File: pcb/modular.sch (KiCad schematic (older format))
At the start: 40 parts

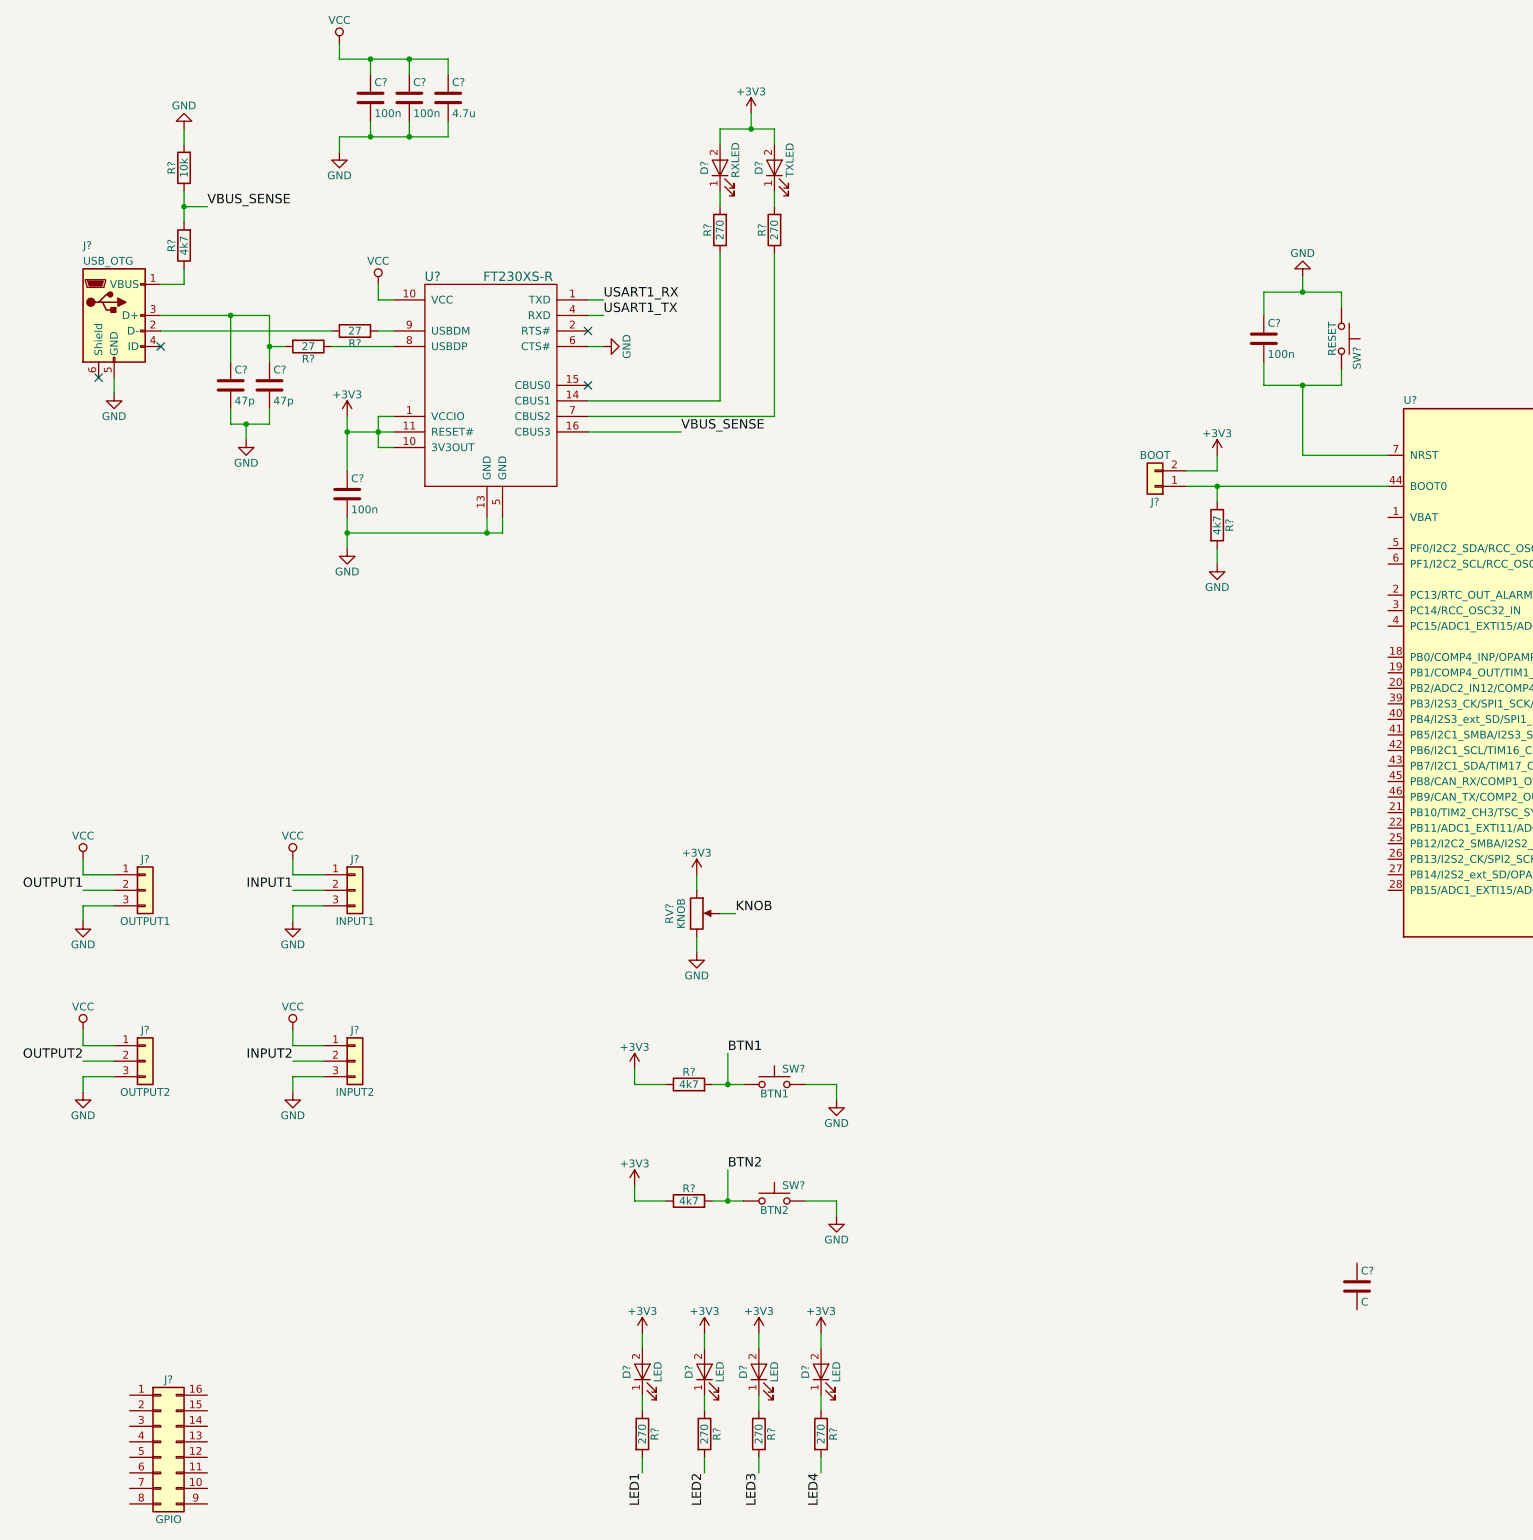
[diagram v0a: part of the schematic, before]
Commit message: Added pcb layout
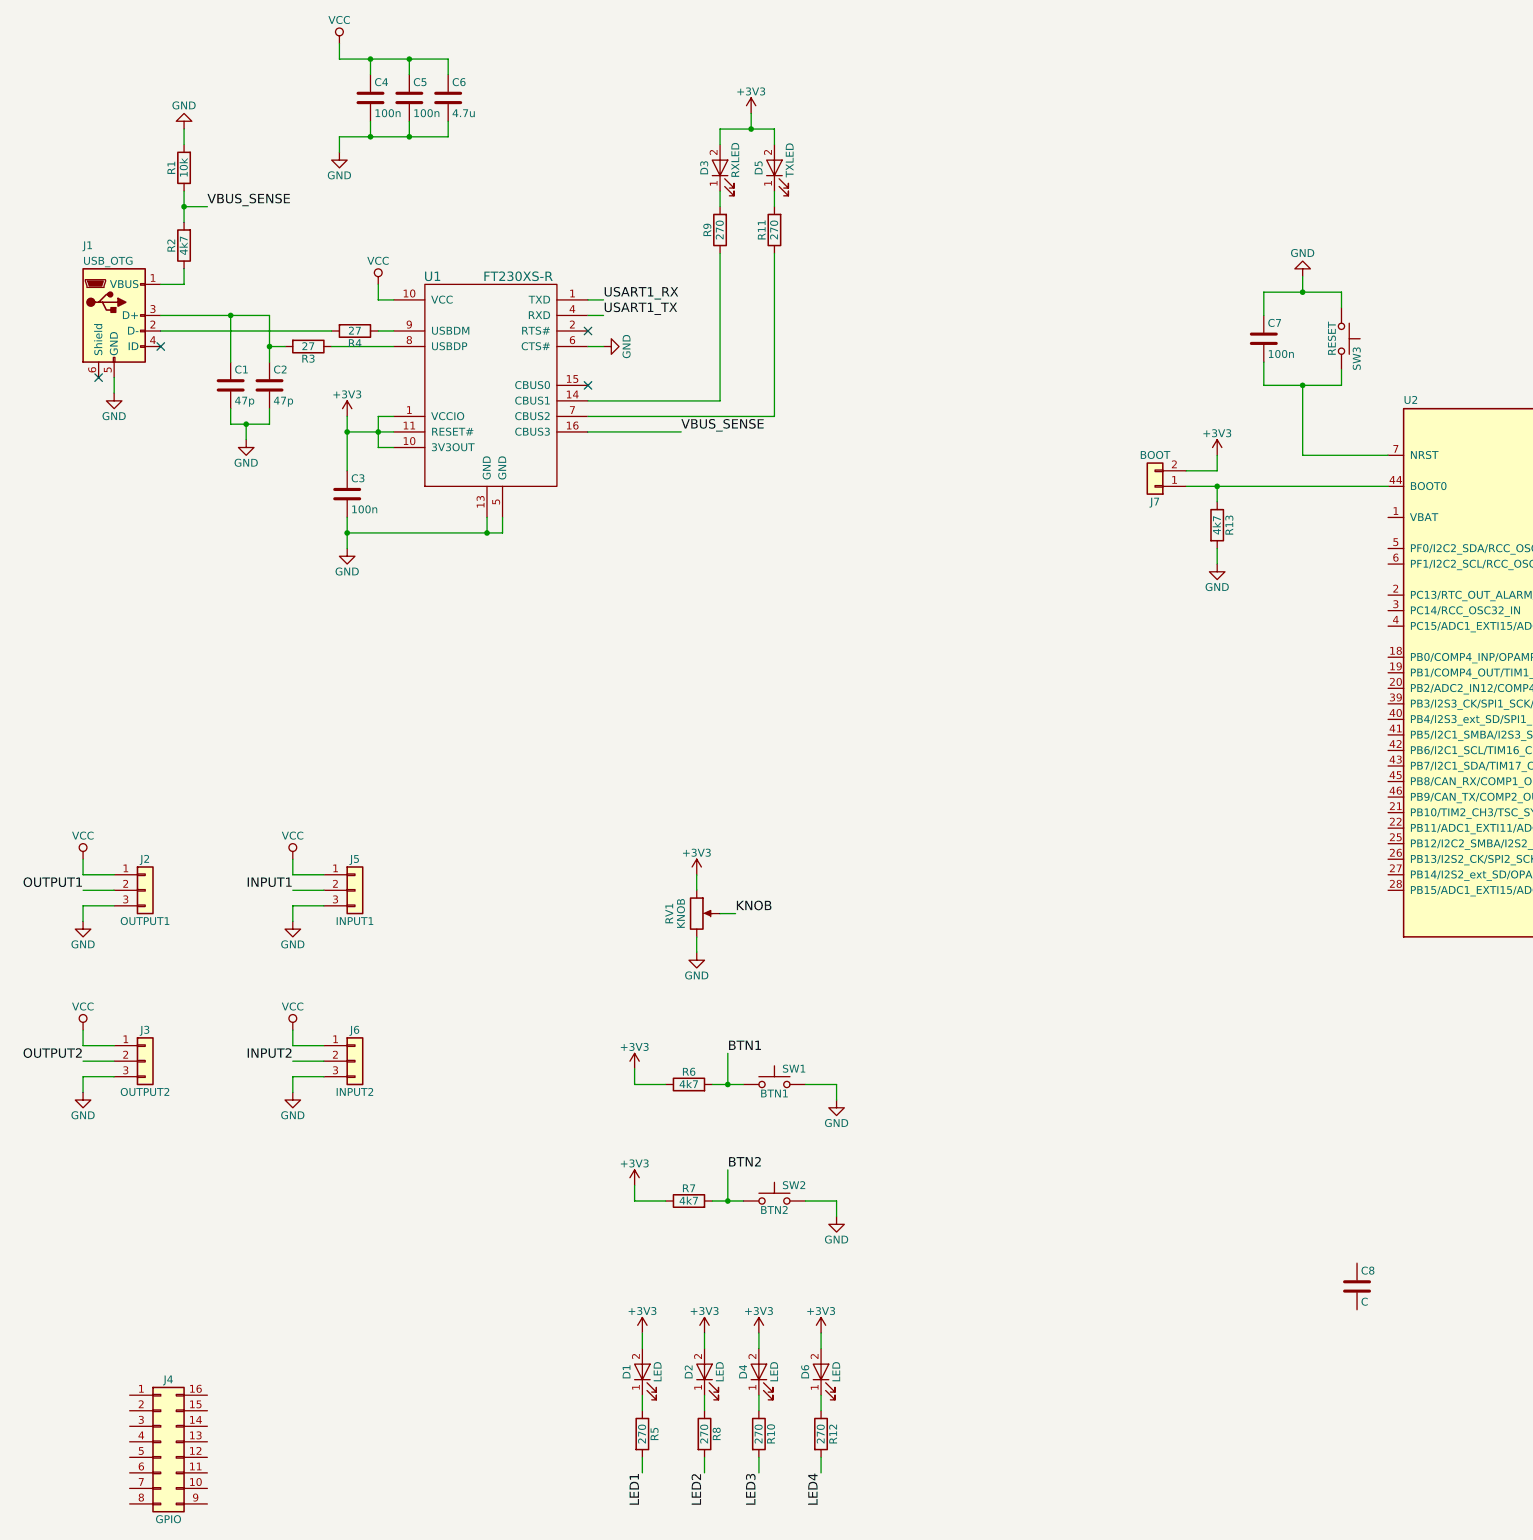
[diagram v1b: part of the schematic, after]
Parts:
- C1, C2, C3, C4, C5, C6, C7, C8: renamed from C?; footprint (none) -> Capacitors_SMD:C_1210_HandSoldering
- D1, D2, D3, D4, D5, D6: renamed from D?; footprint (none) -> LEDs:LED_1206_HandSoldering
- J1: renamed from J?; footprint (none) -> Connectors_USB:USB_Micro-B_Molex-105017-0001
- J2, J3, J5, J6: renamed from J?; footprint (none) -> Pin_Headers:Pin_Header_Straight_1x03_Pitch2.54mm
- J4: renamed from J?; footprint (none) -> Pin_Headers:Pin_Header_Straight_2x08_Pitch2.54mm
- J7: renamed from J?; footprint (none) -> Pin_Headers:Pin_Header_Straight_1x02_Pitch2.54mm
- R1, R10, R11, R12, R13, R2, R3, R4, R5, R6, R7, R8, R9: renamed from R?; footprint (none) -> Resistors_SMD:R_1210_HandSoldering
- RV1: renamed from RV?; footprint (none) -> Potentiometers:Potentiometer_Alps_RK09K_Vertical
- SW1, SW2, SW3: renamed from SW?; footprint (none) -> Buttons_Switches_THT:SW_PUSH_6mm
- U1: renamed from U?; footprint (none) -> Housings_SSOP:SSOP-16_3.9x4.9mm_Pitch0.635mm
- gave numbers to parts that had none: 1

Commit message: Added 1Mbit memory 23lcv1024 to design
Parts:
- added U3: 23lcv1024, Housings_SOIC:SOIC-8_3.9x4.9mm_Pitch1.27mm, symbol 23lcv1024
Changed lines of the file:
@@
 $EndComp
 $Comp
-L GND #PWR01
+L GND #PWR33
 U 1 1 5AC67D07
 P 16100 9400
-F 0 "#PWR01" H 16100 9150 50  0001 C CNN
+F 0 "#PWR33" H 16100 9150 50  0001 C CNN
 F 1 "GND" H 16100 9250 50  0000 C CNN
 F 2 "" H 16100 9400 50  0001 C CNN
@@
 $EndComp
 $Comp
-L +3V3 #PWR02
+L +3V3 #PWR32
 U 1 1 5AC67ED0
 P 16100 5400
-F 0 "#PWR02" H 16100 5250 50  0001 C CNN
+F 0 "#PWR32" H 16100 5250 50  0001 C CNN
 F 1 "+3V3" H 16100 5540 50  0000 C CNN
 F 2 "" H 16100 5400 50  0001 C CNN
@@
 $EndComp
 $Comp
-L GND #PWR03
+L GND #PWR7
 U 1 1 5AC6811D
 P 3300 5900
-F 0 "#PWR03" H 3300 5650 50  0001 C CNN
+F 0 "#PWR7" H 3300 5650 50  0001 C CNN
 F 1 "GND" H 3300 5750 50  0000 C CNN
 F 2 "" H 3300 5900 50  0001 C CNN
@@
 $EndComp
 $Comp
-L GND #PWR04
+L GND #PWR5
 U 1 1 5AC697C1
 P 2450 5600
-F 0 "#PWR04" H 2450 5350 50  0001 C CNN
+F 0 "#PWR5" H 2450 5350 50  0001 C CNN
 F 1 "GND" H 2450 5450 50  0000 C CNN
 F 2 "" H 2450 5600 50  0001 C CNN
@@
 $EndComp
 $Comp
-L GND #PWR05
+L GND #PWR15
 U 1 1 5AC69A78
 P 3950 6600
-F 0 "#PWR05" H 3950 6350 50  0001 C CNN
+F 0 "#PWR15" H 3950 6350 50  0001 C CNN
 F 1 "GND" H 3950 6450 50  0000 C CNN
 F 2 "" H 3950 6600 50  0001 C CNN
@@
 $EndComp
 $Comp
-L GND #PWR06
+L GND #PWR6
 U 1 1 5AC69DBA
 P 2900 3900
-F 0 "#PWR06" H 2900 3650 50  0001 C CNN
+F 0 "#PWR6" H 2900 3650 50  0001 C CNN
 F 1 "GND" H 2900 3750 50  0000 C CNN
 F 2 "" H 2900 3900 50  0001 C CNN
@@
 VBUS_SENSE
 $Comp
-L VCC #PWR07
+L VCC #PWR16
 U 1 1 5AC6A00C
 P 4150 4900
-F 0 "#PWR07" H 4150 4750 50  0001 C CNN
+F 0 "#PWR16" H 4150 4750 50  0001 C CNN
 F 1 "VCC" H 4150 5050 50  0000 C CNN
 F 2 "" H 4150 4900 50  0001 C CNN
@@
 $EndComp
 $Comp
-L VCC #PWR08
+L VCC #PWR12
 U 1 1 5AC6A12C
 P 3900 3350
-F 0 "#PWR08" H 3900 3200 50  0001 C CNN
+F 0 "#PWR12" H 3900 3200 50  0001 C CNN
 F 1 "VCC" H 3900 3500 50  0000 C CNN
 F 2 "" H 3900 3350 50  0001 C CNN
@@
 $EndComp
 $Comp
-L GND #PWR09
+L GND #PWR13
 U 1 1 5AC6A292
 P 3900 4050
-F 0 "#PWR09" H 3900 3800 50  0001 C CNN
+F 0 "#PWR13" H 3900 3800 50  0001 C CNN
 F 1 "GND" H 3900 3900 50  0000 C CNN
 F 2 "" H 3900 4050 50  0001 C CNN
@@
 $EndComp
 $Comp
-L +3V3 #PWR010
+L +3V3 #PWR14
 U 1 1 5AC6AB87
 P 3950 5750
-F 0 "#PWR010" H 3950 5600 50  0001 C CNN
+F 0 "#PWR14" H 3950 5600 50  0001 C CNN
 F 1 "+3V3" H 3950 5890 50  0000 C CNN
 F 2 "" H 3950 5750 50  0001 C CNN
@@
 $EndComp
 $Comp
-L +3V3 #PWR011
+L +3V3 #PWR24
 U 1 1 5AC6ACCE
 P 6550 3800
-F 0 "#PWR011" H 6550 3650 50  0001 C CNN
+F 0 "#PWR24" H 6550 3650 50  0001 C CNN
 F 1 "+3V3" H 6550 3940 50  0000 C CNN
 F 2 "" H 6550 3800 50  0001 C CNN
@@
 NoConn ~ 2750 5300
 $Comp
-L GND #PWR012
+L GND #PWR17
 U 1 1 5AC74DEC
 P 5600 5300
-F 0 "#PWR012" H 5600 5050 50  0001 C CNN
+F 0 "#PWR17" H 5600 5050 50  0001 C CNN
 F 1 "GND" H 5600 5150 50  0000 C CNN
 F 2 "" H 5600 5300 50  0001 C CNN
@@
 $EndComp
 $Comp
-L GND #PWR013
+L GND #PWR2
 U 1 1 5AC8A6E0
 P 2250 9000
-F 0 "#PWR013" H 2250 8750 50  0001 C CNN
+F 0 "#PWR2" H 2250 8750 50  0001 C CNN
 F 1 "GND" H 2250 8850 50  0000 C CNN
 F 2 "" H 2250 9000 50  0001 C CNN
@@
 $EndComp
 $Comp
-L VCC #PWR014
+L VCC #PWR1
 U 1 1 5AC8A733
 P 2250 8600
-F 0 "#PWR014" H 2250 8450 50  0001 C CNN
+F 0 "#PWR1" H 2250 8450 50  0001 C CNN
 F 1 "VCC" H 2250 8750 50  0000 C CNN
 F 2 "" H 2250 8600 50  0001 C CNN
@@
 $EndComp
 $Comp
-L GND #PWR015
+L GND #PWR4
 U 1 1 5AC8A9BD
 P 2250 10100
-F 0 "#PWR015" H 2250 9850 50  0001 C CNN
+F 0 "#PWR4" H 2250 9850 50  0001 C CNN
 F 1 "GND" H 2250 9950 50  0000 C CNN
 F 2 "" H 2250 10100 50  0001 C CNN
@@
 $EndComp
 $Comp
-L VCC #PWR016
+L VCC #PWR3
 U 1 1 5AC8A9C3
 P 2250 9700
-F 0 "#PWR016" H 2250 9550 50  0001 C CNN
+F 0 "#PWR3" H 2250 9550 50  0001 C CNN
 F 1 "VCC" H 2250 9850 50  0000 C CNN
 F 2 "" H 2250 9700 50  0001 C CNN
@@
 $EndComp
 $Comp
-L GND #PWR017
+L GND #PWR9
 U 1 1 5AC8AA9F
 P 3600 9000
-F 0 "#PWR017" H 3600 8750 50  0001 C CNN
+F 0 "#PWR9" H 3600 8750 50  0001 C CNN
 F 1 "GND" H 3600 8850 50  0000 C CNN
 F 2 "" H 3600 9000 50  0001 C CNN
@@
 $EndComp
 $Comp
-L VCC #PWR018
+L VCC #PWR8
 U 1 1 5AC8AAA5
 P 3600 8600
-F 0 "#PWR018" H 3600 8450 50  0001 C CNN
+F 0 "#PWR8" H 3600 8450 50  0001 C CNN
 F 1 "VCC" H 3600 8750 50  0000 C CNN
 F 2 "" H 3600 8600 50  0001 C CNN
@@
 $EndComp
 $Comp
-L GND #PWR019
+L GND #PWR11
 U 1 1 5AC8AAB7
 P 3600 10100
-F 0 "#PWR019" H 3600 9850 50  0001 C CNN
+F 0 "#PWR11" H 3600 9850 50  0001 C CNN
 F 1 "GND" H 3600 9950 50  0000 C CNN
 F 2 "" H 3600 10100 50  0001 C CNN
@@
 $EndComp
 $Comp
-L VCC #PWR020
+L VCC #PWR10
 U 1 1 5AC8AABD
 P 3600 9700
-F 0 "#PWR020" H 3600 9550 50  0001 C CNN
+F 0 "#PWR10" H 3600 9550 50  0001 C CNN
 F 1 "VCC" H 3600 9850 50  0000 C CNN
 F 2 "" H 3600 9700 50  0001 C CNN
@@
 	3600 9900 3800 9900
 $Comp
-L +3V3 #PWR021
+L +3V3 #PWR21
 U 1 1 5AC8B675
 P 6200 8700
-F 0 "#PWR021" H 6200 8550 50  0001 C CNN
+F 0 "#PWR21" H 6200 8550 50  0001 C CNN
 F 1 "+3V3" H 6200 8840 50  0000 C CNN
 F 2 "" H 6200 8700 50  0001 C CNN
@@
 $EndComp
 $Comp
-L GND #PWR022
+L GND #PWR22
 U 1 1 5AC8B6CB
 P 6200 9200
-F 0 "#PWR022" H 6200 8950 50  0001 C CNN
+F 0 "#PWR22" H 6200 8950 50  0001 C CNN
 F 1 "GND" H 6200 9050 50  0000 C CNN
 F 2 "" H 6200 9200 50  0001 C CNN
@@
 $EndComp
 $Comp
-L GND #PWR023
+L GND #PWR27
 U 1 1 5AC8CB6B
 P 7100 10150
-F 0 "#PWR023" H 7100 9900 50  0001 C CNN
+F 0 "#PWR27" H 7100 9900 50  0001 C CNN
 F 1 "GND" H 7100 10000 50  0000 C CNN
 F 2 "" H 7100 10150 50  0001 C CNN
@@
 $EndComp
 $Comp
-L +3V3 #PWR024
+L +3V3 #PWR18
 U 1 1 5AC8CBC7
 P 5800 9950
-F 0 "#PWR024" H 5800 9800 50  0001 C CNN
+F 0 "#PWR18" H 5800 9800 50  0001 C CNN
 F 1 "+3V3" H 5800 10090 50  0000 C CNN
 F 2 "" H 5800 9950 50  0001 C CNN
@@
 $EndComp
 $Comp
-L GND #PWR025
+L GND #PWR28
 U 1 1 5AC8D209
 P 7100 10900
-F 0 "#PWR025" H 7100 10650 50  0001 C CNN
+F 0 "#PWR28" H 7100 10650 50  0001 C CNN
 F 1 "GND" H 7100 10750 50  0000 C CNN
 F 2 "" H 7100 10900 50  0001 C CNN
@@
 $EndComp
 $Comp
-L +3V3 #PWR026
+L +3V3 #PWR19
 U 1 1 5AC8D20F
 P 5800 10700
-F 0 "#PWR026" H 5800 10550 50  0001 C CNN
+F 0 "#PWR19" H 5800 10550 50  0001 C CNN
 F 1 "+3V3" H 5800 10840 50  0000 C CNN
 F 2 "" H 5800 10700 50  0001 C CNN
@@
 $EndComp
 $Comp
-L +3V3 #PWR027
+L +3V3 #PWR23
 U 1 1 5AC8DAD0
 P 6250 11650
-F 0 "#PWR027" H 6250 11500 50  0001 C CNN
+F 0 "#PWR23" H 6250 11500 50  0001 C CNN
 F 1 "+3V3" H 6250 11790 50  0000 C CNN
 F 2 "" H 6250 11650 50  0001 C CNN
@@
 $EndComp
 $Comp
-L +3V3 #PWR028
+L +3V3 #PWR20
 U 1 1 5AC8E142
 P 5850 11650
-F 0 "#PWR028" H 5850 11500 50  0001 C CNN
+F 0 "#PWR20" H 5850 11500 50  0001 C CNN
 F 1 "+3V3" H 5850 11790 50  0000 C CNN
 F 2 "" H 5850 11650 50  0001 C CNN
@@
 $EndComp
 $Comp
-L +3V3 #PWR029
+L +3V3 #PWR26
 U 1 1 5AC8E1CA
 P 7000 11650
-F 0 "#PWR029" H 7000 11500 50  0001 C CNN
+F 0 "#PWR26" H 7000 11500 50  0001 C CNN
 F 1 "+3V3" H 7000 11790 50  0000 C CNN
 F 2 "" H 7000 11650 50  0001 C CNN
@@
 $EndComp
 $Comp
-L +3V3 #PWR030
+L +3V3 #PWR25
 U 1 1 5AC8E1DE
 P 6600 11650
-F 0 "#PWR030" H 6600 11500 50  0001 C CNN
+F 0 "#PWR25" H 6600 11500 50  0001 C CNN
 F 1 "+3V3" H 6600 11790 50  0000 C CNN
 F 2 "" H 6600 11650 50  0001 C CNN
@@
 $EndComp
 $Comp
-L GND #PWR031
+L GND #PWR30
 U 1 1 5AC8F51E
 P 9550 6700
-F 0 "#PWR031" H 9550 6450 50  0001 C CNN
+F 0 "#PWR30" H 9550 6450 50  0001 C CNN
 F 1 "GND" H 9550 6550 50  0000 C CNN
 F 2 "" H 9550 6700 50  0001 C CNN
@@
 Connection ~ 9550 6200
 $Comp
-L +3V3 #PWR032
+L +3V3 #PWR29
 U 1 1 5AC8FA74
 P 9550 6000
-F 0 "#PWR032" H 9550 5850 50  0001 C CNN
+F 0 "#PWR29" H 9550 5850 50  0001 C CNN
 F 1 "+3V3" H 9550 6140 50  0000 C CNN
 F 2 "" H 9550 6000 50  0001 C CNN
@@
 	9850 5550 9850 5400
 $Comp
-L GND #PWR033
+L GND #PWR31
 U 1 1 5AC90E82
 P 10100 4850
-F 0 "#PWR033" H 10100 4600 50  0001 C CNN
+F 0 "#PWR31" H 10100 4600 50  0001 C CNN
 F 1 "GND" H 10100 4700 50  0000 C CNN
 F 2 "" H 10100 4850 50  0001 C CNN
@@
 	10100 6000 10650 6000
 Connection ~ 10100 5550
+$Comp
+L 23lcv1024 U3
+U 1 1 5BD6EECB
+P 13650 11700
+F 0 "U3" H 13400 12000 60  0000 C CNN
+F 1 "23lcv1024" H 13750 11400 60  0000 C CNN
+F 2 "Housings_SOIC:SOIC-8_3.9x4.9mm_Pitch1.27mm" H 13650 11700 60  0001 C CNN
+F 3 "" H 13650 11700 60  0001 C CNN
+	1    13650 11700
+	1    0    0    -1
+$EndComp
+$Comp
+L +3V3 #PWR?
+U 1 1 5BD730D3
+P 14500 11400
+F 0 "#PWR?" H 14500 11250 50  0001 C CNN
+F 1 "+3V3" H 14500 11540 50  0000 C CNN
+F 2 "" H 14500 11400 50  0001 C CNN
+F 3 "" H 14500 11400 50  0001 C CNN
+	1    14500 11400
+	1    0    0    -1
+$EndComp
+$Comp
+L GND #PWR?
+U 1 1 5BD73159
+P 13000 12050
+F 0 "#PWR?" H 13000 11800 50  0001 C CNN
+F 1 "GND" H 13000 11900 50  0000 C CNN
+F 2 "" H 13000 12050 50  0001 C CNN
+F 3 "" H 13000 12050 50  0001 C CNN
+	1    13000 12050
+	1    0    0    -1
+$EndComp
 $EndSCHEMATC
